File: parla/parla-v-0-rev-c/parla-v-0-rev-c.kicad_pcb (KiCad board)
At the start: 2 copper layers, 50 x 50 mm, 29 parts, among them J1 AudioJack2_SwitchT, J2 AudioJack2_SwitchT, J3 AudioJack2_SwitchT, J4 AudioJack2_SwitchT, J5 Barrel_Jack_Switch, SW3 SW_SPDT, U1 PAM8403D, U2 L7805

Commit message: avances en eurorack
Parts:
- removed C7: 100u, Capacitor_SMD:CP_Elec_5x5.4
- removed D1: 1N4007, Diode_SMD:D_SOD-323_HandSoldering
- removed D8: LED, LED_THT:LED_D5.0mm
- removed H1, H2, H3, H4: M3, MountingHole:MountingHole_3.2mm_M3
- removed J5: Barrel_Jack_Switch, Connector_BarrelJack:BarrelJack_Horizontal
- removed R5: 1k, Resistor_SMD:R_0805_2012Metric_Pad1.20x1.40mm_HandSolder
- removed SW3: SW_SPDT, dis8644:spdt_ssd12d00g3
- added D2: D_Schottky, easyeda2kicad:SOD-123FL_L2.8-W1.8-LS3.7-R-RD, F.Cu at (56.4, 78.8)
- added D3: D_Schottky, easyeda2kicad:SOD-123FL_L2.8-W1.8-LS3.7-R-RD, F.Cu at (62.3, 78.8)
- added J6: Conn_02x05_Odd_Even, Connector_IDC:IDC-Header_2x05_P2.54mm_Vertical, B.Cu at (58.0, 71.1)
- J1, J2, J3, J4: footprint dis8644:PJ301M-12-T_TN_S -> BYOM_General:Jack_3.5mm_QingPu_WQP-PJ398SM_Vertical
- RV1, RV2: footprint Potentiometer_THT:Potentiometer_Bourns_PTV09A-1_Single_Vertical -> BYOM_General:POT_TH_Alps_RK09K_Single_Vertical
- moved J3 85.9 mm to (57.5, 155.9), turned to 0 degrees
- moved J1 78.0 mm to (57.7, 139.8), turned to 0 degrees
- moved J4 77.6 mm to (70.0, 155.9), turned to 0 degrees
- moved J2 64.3 mm to (70.2, 139.8), turned to 0 degrees
- moved C4 52.9 mm to (60.6, 128.2), turned to 0 degrees
- moved R4 48.8 mm to (65.4, 128.4), turned to 0 degrees
- moved C9 47.5 mm to (72.7, 127.5)
- moved C3 47.0 mm to (54.3, 126.1), turned to 180 degrees
- moved U1 44.7 mm to (63.4, 121.0)
- moved U2 42.4 mm to (57.0, 85.8)
- moved C5 41.5 mm to (69.5, 114.6)
- moved C6 41.5 mm to (73.3, 114.6)
- moved R3 41.1 mm to (54.2, 123.1)
- moved C2 39.4 mm to (72.7, 120.3)
- moved C10 31.8 mm to (66.0, 89.1)
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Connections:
- J1 pad S: GND -> Net-(U1-LOUT-)
- J2 pad S: GND -> Net-(U1-ROUT-)
- J3 pad TN: unconnected-(J3-PadTN) -> GND
- J4 pad TN: unconnected-(J4-PadTN) -> GND
- U1 pad 14: GND -> Net-(U1-ROUT-)
- U1 pad 3: GND -> Net-(U1-LOUT-)
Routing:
- net +5V: track 90.1 -> 0.00 mm
- net Net-(J4-PadT): track 44.1 -> 0.00 mm
- net Net-(U1-LOUT+): track 41.8 -> 0.00 mm, vias 1 -> 0
- net Net-(J3-PadT): track 39.3 -> 0.00 mm
- net Net-(U1-ROUT+): track 30.1 -> 0.00 mm, vias 1 -> 0
- net Net-(U1-INR): track 21.6 -> 0.00 mm, vias 2 -> 0
- net +12V: track 20.9 -> 0.00 mm
- net Net-(C1-Pad1): track 20.3 -> 0.00 mm
- net Net-(C2-Pad1): track 18.9 -> 0.00 mm
- net Net-(C1-Pad2): track 18.6 -> 0.00 mm, vias 2 -> 0
- net GND: track 18.2 -> 0.00 mm
- net Net-(U1-INL): track 14.5 -> 0.00 mm
- net Net-(SW3-A): track 14.3 -> 0.00 mm
- net Net-(C2-Pad2): track 13.9 -> 0.00 mm
- net Net-(D8-K): track 10.1 -> 0.00 mm, vias 1 -> 0
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- removed copper zone on B.Cu, net GND
- removed copper zone on F.Cu, net GND
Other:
- board size 50 x 50 mm -> 27.5 x 100 mm
- board text removed: "IN"
- board text removed: "L"
- board text removed: "OUT"
- board text removed: "R"

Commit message: agregar mas avances en eurorack
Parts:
- removed C10: 100n, Capacitor_SMD:C_0805_2012Metric_Pad1.18x1.45mm_HandSolder
- removed C8: 220u, Capacitor_SMD:CP_Elec_6.3x7.7
- removed C9: 10u, Capacitor_SMD:CP_Elec_4x5.4
- removed D3: D_Schottky, easyeda2kicad:SOD-123FL_L2.8-W1.8-LS3.7-R-RD
- removed J6: Conn_02x05_Odd_Even, Connector_IDC:IDC-Header_2x05_P2.54mm_Vertical
- removed R3, R4: 10k, Resistor_SMD:R_0805_2012Metric_Pad1.20x1.40mm_HandSolder
- added D1: D_Schottky, easyeda2kicad:SOD-123FL_L2.8-W1.8-LS3.7-R-RD, F.Cu at (69.7, 63.0)
- added J5: AudioJack2_SwitchT, BYOM_General:Jack_3.5mm_QingPu_WQP-PJ398SM_Vertical, F.Cu at (68.6, 141.0)
- added R1: 10k, Resistor_SMD:R_0805_2012Metric_Pad1.20x1.40mm_HandSolder, F.Cu at (72.0, 84.0)
- added R2: 10k, Resistor_SMD:R_0805_2012Metric_Pad1.20x1.40mm_HandSolder, F.Cu at (72.0, 87.0)
- C4: value 1u -> 10u; footprint Capacitor_SMD:C_0805_2012Metric_Pad1.18x1.45mm_HandSolder -> Capacitor_SMD:CP_Elec_4x5.4
- C5: value 1u -> 100n
- C6: value 1u -> 220u; footprint Capacitor_SMD:C_0805_2012Metric_Pad1.18x1.45mm_HandSolder -> Capacitor_SMD:CP_Elec_6.3x7.7
- J1: value AudioJack2_SwitchT -> Conn_02x05_Odd_Even; footprint BYOM_General:Jack_3.5mm_QingPu_WQP-PJ398SM_Vertical -> Connector_IDC:IDC-Header_2x05_P2.54mm_Vertical; moved to B.Cu
- U1: value PAM8403D -> L7805; footprint Package_SO:SOP-16_4.4x10.4mm_P1.27mm -> Package_TO_SOT_SMD:TO-252-2
- U2: value L7805 -> PAM8403D; footprint Package_TO_SOT_SMD:TO-252-2 -> Package_SO:SOP-16_4.4x10.4mm_P1.27mm
- moved J1 84.8 mm to (57.6, 55.0), turned to -90 degrees
- moved C4 58.1 mm to (71.0, 71.0), turned to -90 degrees
- moved C3 56.1 mm to (55.0, 70.0), turned to 0 degrees
- moved U1 54.7 mm to (63.0, 66.3), turned to 90 degrees
- moved C5 37.7 mm to (71.0, 77.0), turned to 0 degrees
- moved C1 34.2 mm to (54.0, 83.0)
- moved J3 32.9 mm to (68.6, 124.9)
- moved C2 21.8 mm to (70.0, 98.7)
- moved J2 20.1 mm to (56.6, 125.0)
- moved J4 20.0 mm to (56.6, 141.1)
- moved D2 15.8 mm to (56.2, 63.0)
- moved RV2 14.9 mm to (59.0, 93.3)
- moved U2 7.46 mm to (62.7, 81.0), turned to 0 degrees
- moved RV1 6.16 mm to (59.0, 109.1)
- moved C6 5.14 mm to (70.0, 110.7)
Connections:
- C3 pad 1: Net-(U1-VREF) -> Net-(U2-VREF)
- C4 pad 1: GND -> +5V
- C4 pad 2: +5V -> GND
- C5 pad 1: GND -> +5V
- C5 pad 2: +5V -> GND
- C6 pad 1: GND -> +5V
- C6 pad 2: +5V -> GND
- J2 pad S: Net-(U1-ROUT-) -> GND
- J2 pad T: Net-(U1-ROUT+) -> Net-(J2-PadT)
- J2 pad TN: unconnected-(J2-PadTN) -> GND
- J4 pad S: GND -> Net-(U2-LOUT-)
- J4 pad T: Net-(J4-PadT) -> Net-(U2-LOUT+)
- J4 pad TN: GND -> unconnected-(J4-PadTN)
- RV1 pad 1: Net-(J3-PadT) -> Net-(J2-PadT)
- RV2 pad 1: Net-(J4-PadT) -> Net-(J3-PadT)
- U1 pad 1: Net-(U1-LOUT+) -> +12V
- U1 pad 3: Net-(U1-LOUT-) -> +5V
- U2 pad 1: +12V -> Net-(U2-LOUT+)
- U2 pad 3: +5V -> Net-(U2-LOUT-)
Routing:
- net +5V: track 0.00 -> 49.3 mm
- net Net-(C1-Pad1): track 0.00 -> 38.8 mm
- net Net-(J3-PadT): track 0.00 -> 23.5 mm
- net Net-(U2-VREF): track 0.00 -> 22.0 mm
- net +12V: track 0.00 -> 15.6 mm
- net Net-(C2-Pad1): track 0.00 -> 12.6 mm
- net Net-(D1-A): track 0.00 -> 8.13 mm
- net Net-(D2-K): track 0.00 -> 8.07 mm
- net Net-(U2-LOUT-): track 0.00 -> 6.53 mm
- net Net-(J2-PadT): track 0.00 -> 6.31 mm
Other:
- board size 27.5 x 100 mm -> 25.4 x 100 mm
- board text added: "v0.1 rev C 2026-09"
- board text removed: "rev B 06-2026"

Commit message: cambiar conector
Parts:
- J1: footprint Connector_IDC:IDC-Header_2x05_P2.54mm_Vertical -> BYOM_General:IDC-Header_2x05_P2.54mm_Vertical
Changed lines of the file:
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@@
 		)
 	)
-	(footprint "Connector_IDC:IDC-Header_2x05_P2.54mm_Vertical"
+	(footprint "BYOM_General:IDC-Header_2x05_P2.54mm_Vertical"
 		(layer "B.Cu")
 		(at 57.62 55 -90)

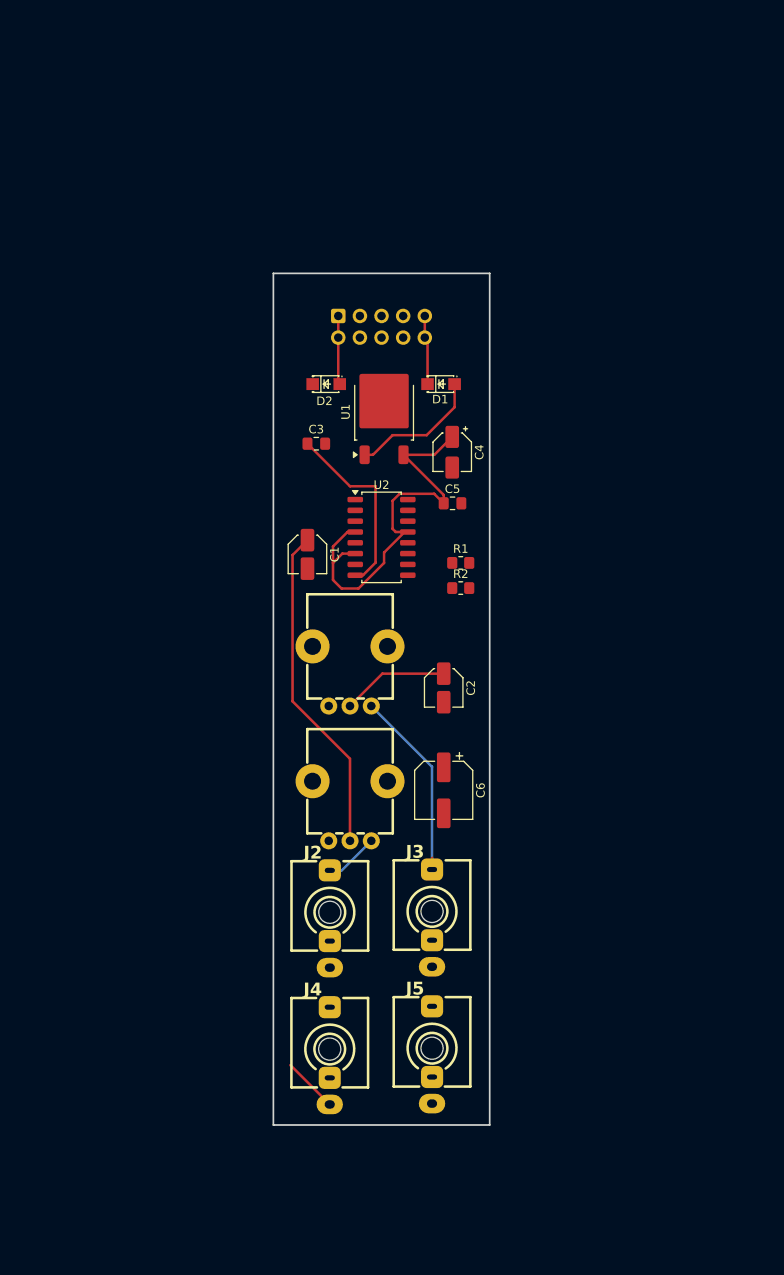
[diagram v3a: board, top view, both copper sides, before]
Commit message: renombrar a versiones consistentes
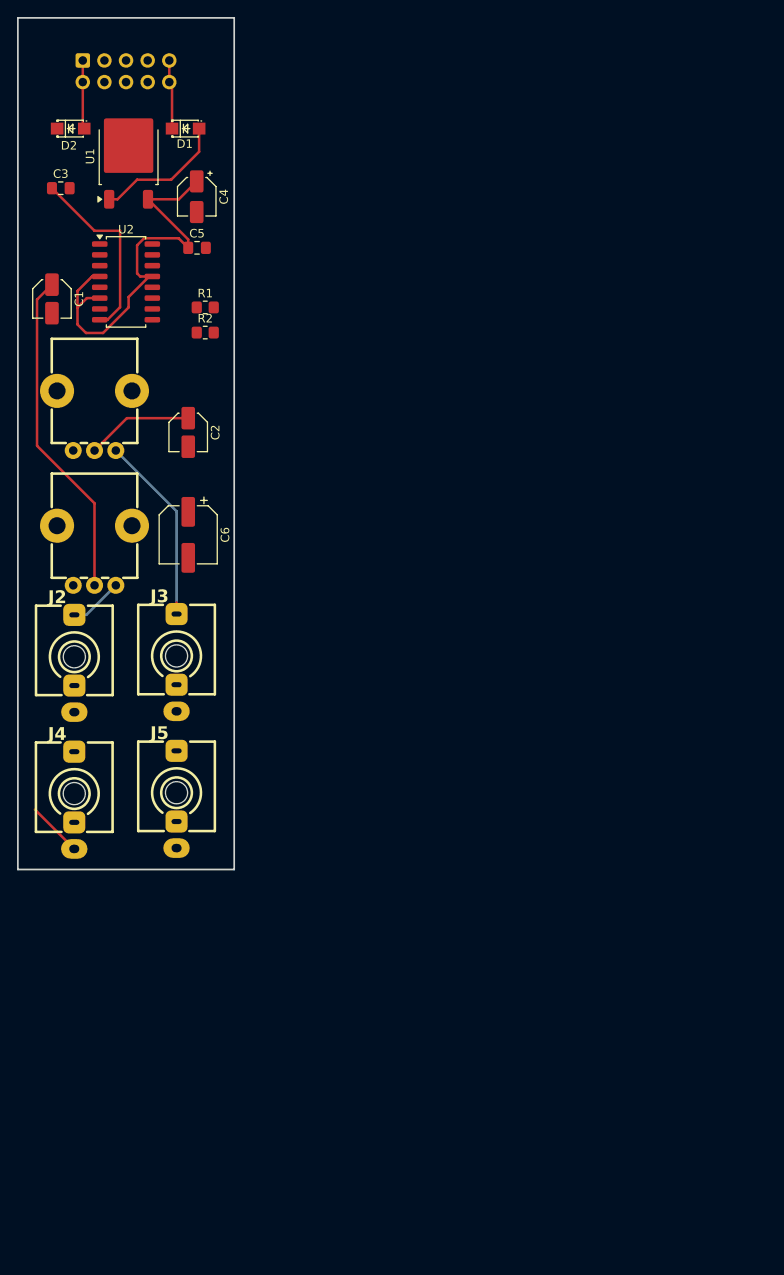
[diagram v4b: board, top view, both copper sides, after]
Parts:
- moved J4 42.4 mm to (26.6, 111.1)
- moved U1 42.4 mm to (33.0, 36.3)
- moved C1 42.4 mm to (24.0, 53.0)
- moved C2 42.4 mm to (40.0, 68.7)
- moved C3 42.4 mm to (25.0, 40.0)
- moved C4 42.4 mm to (41.0, 41.0)
- moved C6 42.4 mm to (40.0, 80.7)
- moved D1 42.4 mm to (39.7, 33.0)
- moved D2 42.4 mm to (26.2, 33.0)
- moved J2 42.4 mm to (26.6, 95.0)
- moved R1 42.4 mm to (42.0, 54.0)
- moved R2 42.4 mm to (42.0, 57.0)
- moved RV1 42.4 mm to (29.0, 79.1)
- moved RV2 42.4 mm to (29.0, 63.3)
- moved U2 42.4 mm to (32.7, 51.0)
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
